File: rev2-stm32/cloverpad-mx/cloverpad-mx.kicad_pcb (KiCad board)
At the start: 2 copper layers, 31 parts, among them J1 USB_C_Receptacle_USB2.0_16P, J2 Conn_01x04, SW1 SW_SPST, SW2 SW_SPST, U1 STM32F072CBT6, U2 XC6206PxxxMR, Y1 16MHz

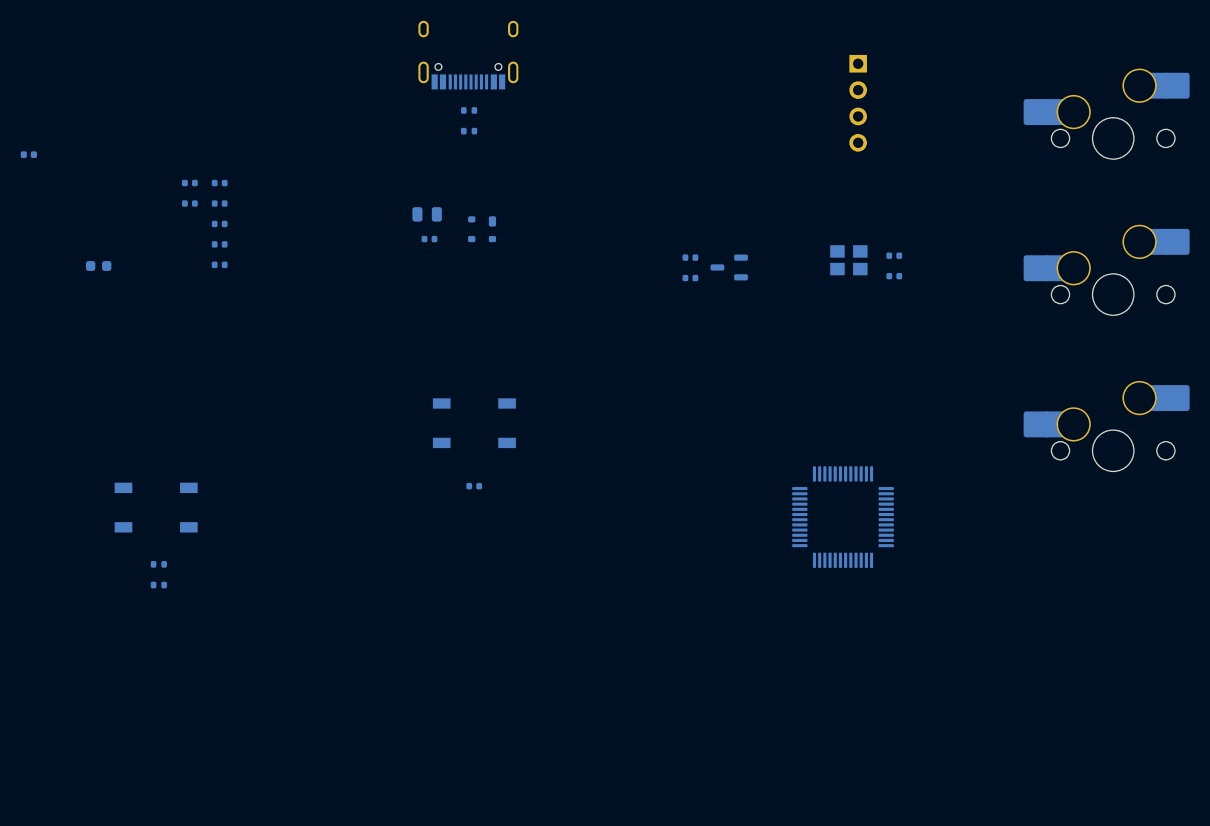
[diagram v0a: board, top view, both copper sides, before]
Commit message: refactor: tidy up rev2-stm32 schematic
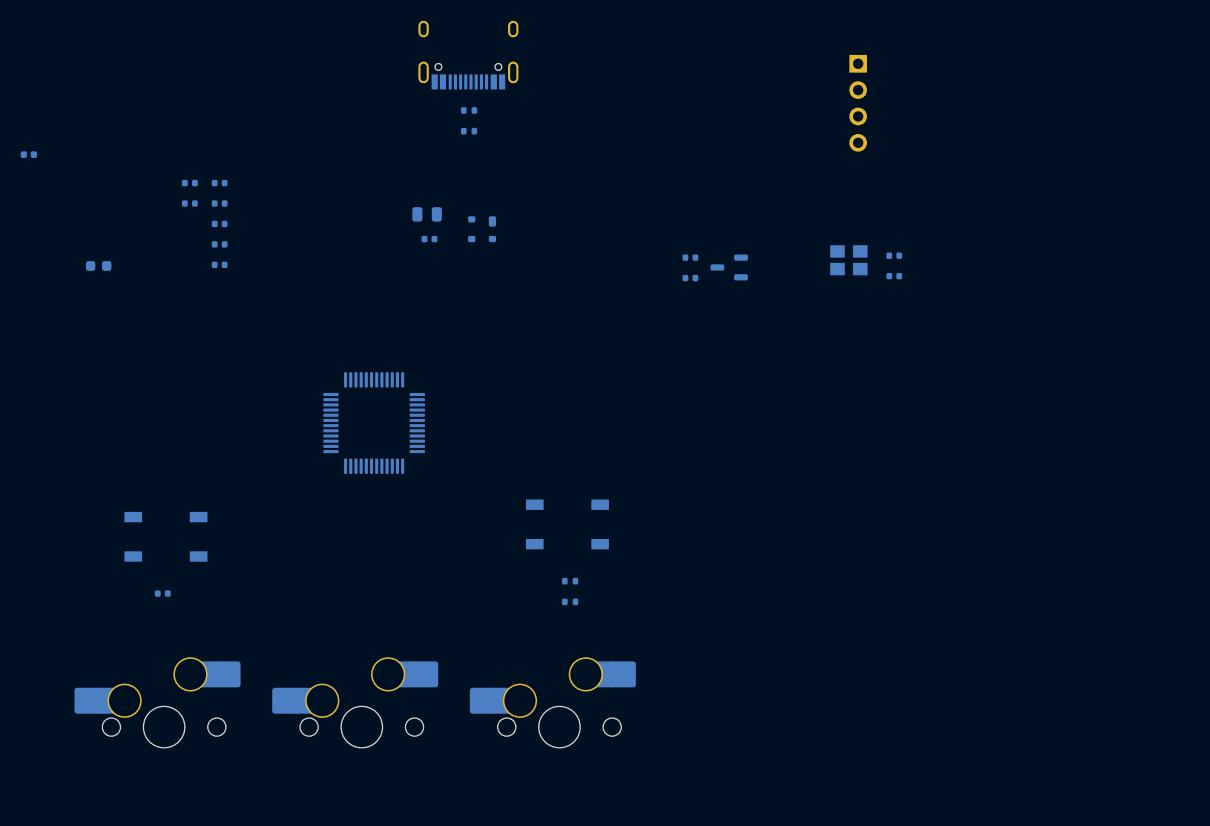
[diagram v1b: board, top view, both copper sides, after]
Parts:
- moved MX1 107.6 mm to (40.5, 89.3)
- moved MX2 83.6 mm to (59.5, 89.3)
- moved MX3 59.6 mm to (78.6, 89.3)
- moved U1 46.1 mm to (60.7, 60.0), turned to 90 degrees
- moved R3 39.7 mm to (79.6, 75.2)
- moved R4 39.7 mm to (79.6, 77.2)
- moved SW1 39.7 mm to (79.4, 69.8)
- moved C14 31.7 mm to (40.3, 76.4)
- moved SW2 31.7 mm to (40.7, 71.0)
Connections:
- net VBUS renamed Net-(F1-Pad1)
- SW1 pad 1: +3.3V -> BOOT0
- SW1 pad 2: BOOT0 -> +3.3V

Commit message: feat: add m2 mounting holes to rev2-stm32 PCB
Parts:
- added H1: Mounting Hole, MountingHole:MountingHole_2.2mm_M2_Pad, B.Cu at (106.6, 76.8)
- added H2: Mounting Hole, MountingHole:MountingHole_2.2mm_M2_Pad, B.Cu at (106.6, 82.7)
- added H3: Mounting Hole, MountingHole:MountingHole_2.2mm_M2_Pad, B.Cu at (106.6, 88.7)
- added H4: Mounting Hole, MountingHole:MountingHole_2.2mm_M2_Pad, B.Cu at (106.6, 94.6)

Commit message: refactor: re-annotate components on rev2-stm32 PCB
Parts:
- renumbered C3 to C1, C12 to C10, C2 to C12, C1 to C13, C4 to C2, C13 to C3, C5 to C4, C6 to C5, C7 to C6, C8 to C7, C9 to C8, C10 to C9, SW2 to SW1, SW1 to SW2, U2 to U1, U1 to U2

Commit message: refactor: swap f072 with f401 has higher performance and on JLC, it doesn't cost much more. will need this for the ADC functionality later
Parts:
- added C10: 100nF, Capacitor_SMD:C_0402_1005Metric, B.Cu at (46.0, 46.4)
- added C16: 2.2uF, Capacitor_SMD:C_0603_1608Metric, B.Cu at (55.2, 65.2)
- U2: value STM32F072CBT6 -> STM32F401RCTx; footprint Package_QFP:LQFP-48_7x7mm_P0.5mm -> Package_QFP:LQFP-64_10x10mm_P0.5mm
- moved U2 3.64 mm to (59.5, 56.6), turned to 135 degrees
- renumbered C10 to C11, C11 to C12, C12 to C13, C13 to C14, C14 to C15
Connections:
- U2 pad 12: unconnected-(U2-PA2-Pad12) -> GND
- U2 pad 13: unconnected-(U2-PA3-Pad13) -> +3.3VA
- U2 pad 18: unconnected-(U2-PB0-Pad18) -> GND
- U2 pad 19: unconnected-(U2-PB1-Pad19) -> +3.3V
- U2 pad 23: GND -> unconnected-(U2-PA7-Pad23)
- U2 pad 24: +3.3V -> unconnected-(U2-PC4-Pad24)
- U2 pad 30: unconnected-(U2-PA9-Pad30) -> Net-(U2-VCAP1)
- U2 pad 31: unconnected-(U2-PA10-Pad31) -> GND
- U2 pad 32: D- -> +3.3V
- U2 pad 33: D+ -> unconnected-(U2-PB12-Pad33)
- U2 pad 34: SWDIO -> unconnected-(U2-PB13-Pad34)
- U2 pad 35: GND -> unconnected-(U2-PB14-Pad35)
- U2 pad 36: +3.3V -> unconnected-(U2-PB15-Pad36)
- U2 pad 37: SWCLK -> unconnected-(U2-PC6-Pad37)
- U2 pad 44: BOOT0 -> D-
- U2 pad 45: unconnected-(U2-PB8-Pad45) -> D+
- U2 pad 46: unconnected-(U2-PB9-Pad46) -> SWDIO
- U2 pad 8: GND -> unconnected-(U2-PC0-Pad8)
- U2 pad 9: +3.3VA -> unconnected-(U2-PC1-Pad9)
